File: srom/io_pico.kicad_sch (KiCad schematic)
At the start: 3 parts, among them U201 Pico-rp2040

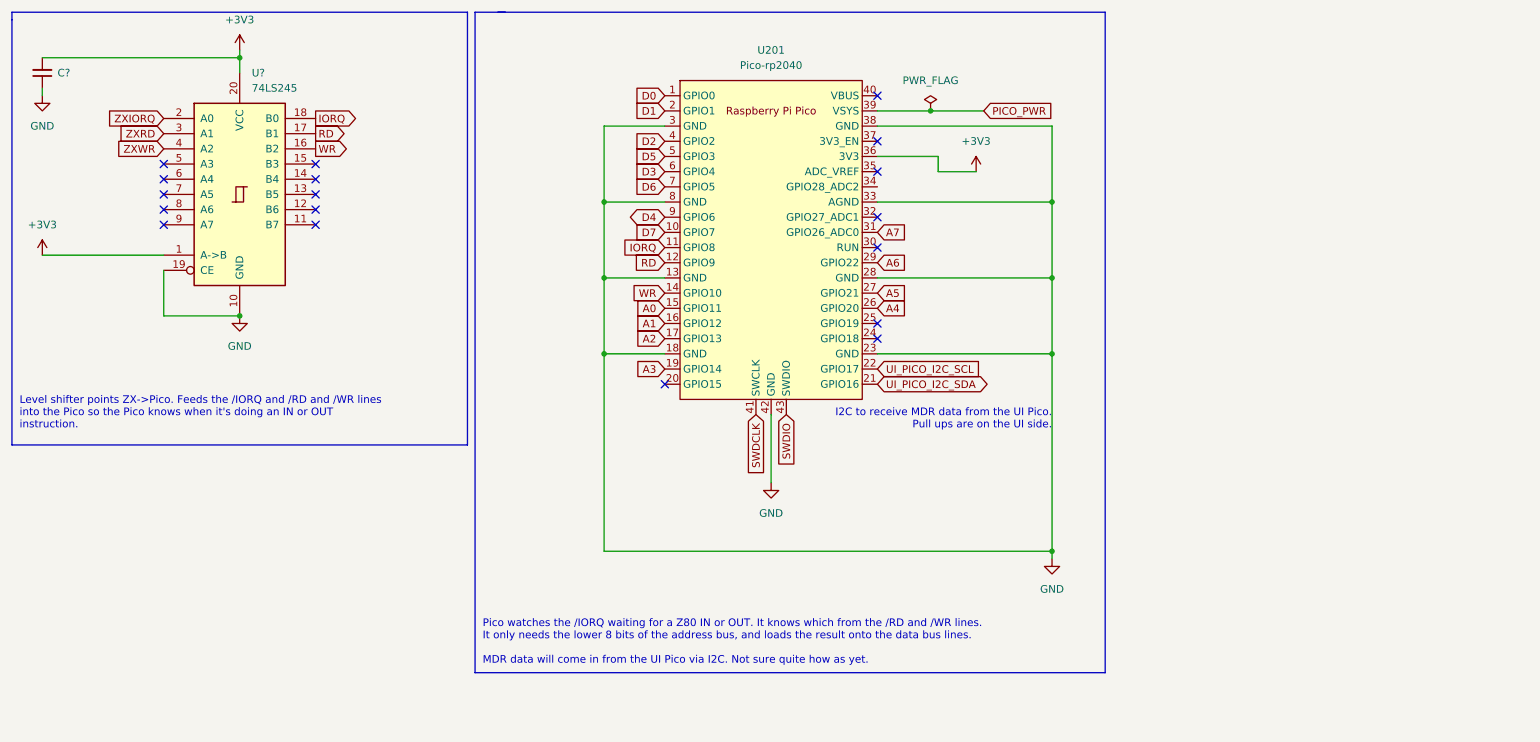
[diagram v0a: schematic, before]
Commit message: schematics complete for IO and UI picos
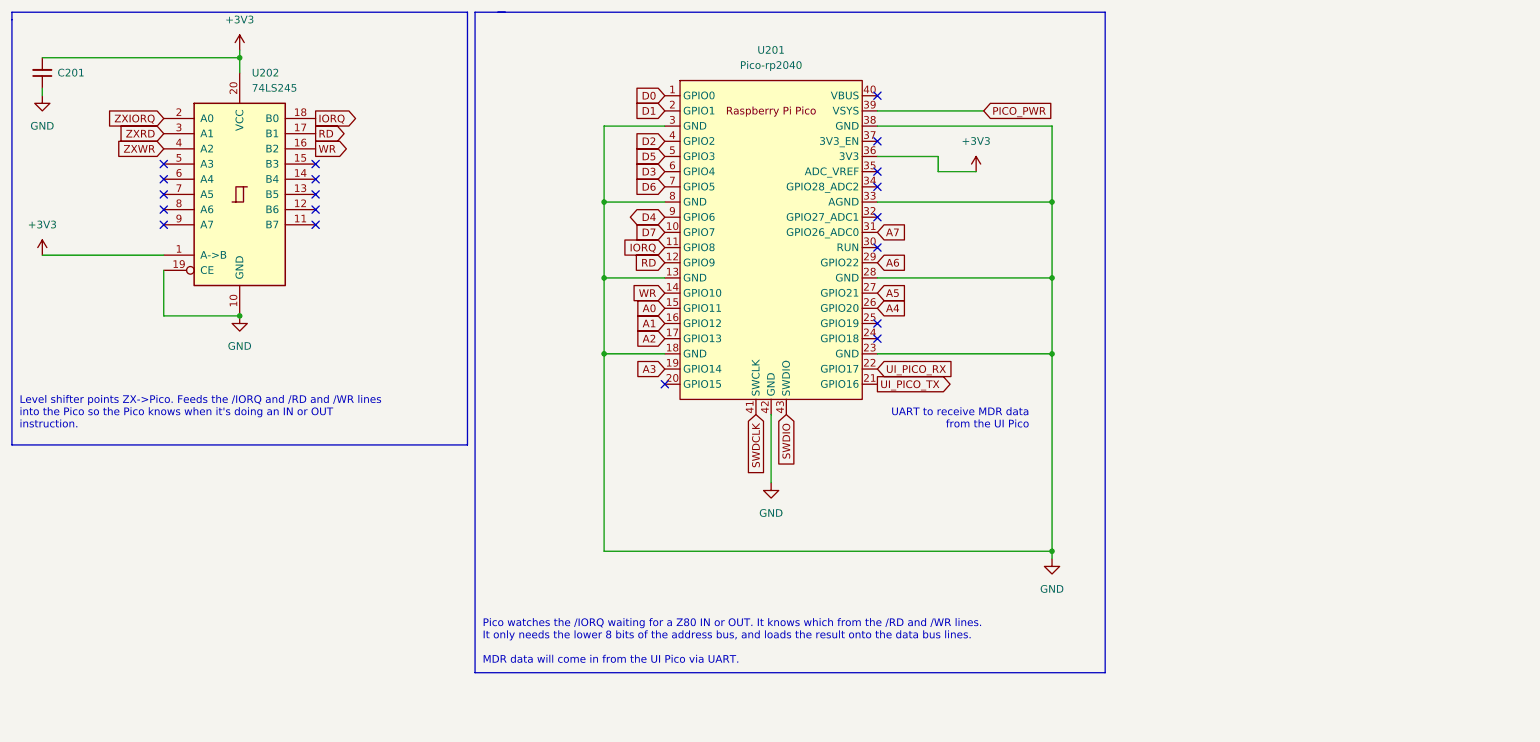
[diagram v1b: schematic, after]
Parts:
- gave numbers to parts that had none: 2
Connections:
- net UI_PICO_I2C_SCL renamed UI_PICO_RX
- net UI_PICO_I2C_SDA renamed UI_PICO_TX
- no-connect marks 18 -> 19
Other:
- note added: "Pico watches the /IORQ waiting for a Z80 IN or OUT. It knows which from the /RD and /WR lines. It only needs the lower 8 bits of the address bus, and loads the result onto the data bus lines. MDR data will come in from the UI Pico via UART."
- note added: "UART to receive MDR data from the UI Pico"
- note removed: "I2C to receive MDR data from the UI Pico. Pull ups are on the UI side."
- note removed: "Pico watches the /IORQ waiting for a Z80 IN or OUT. It knows which from the /RD and /WR lines. It only needs the lower 8 bits of the address bus, and loads the result onto the data bus lines. MDR data will come in from the UI Pico via I2C. Not sure quite how as yet."
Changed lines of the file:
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@@
   (junction (at 191.77 80.01) (diameter 0) (color 0 0 0 0)
-  )
-  (junction (at 171.45 52.07) (diameter 0) (color 0 0 0 0)
   )
   (no_connect (at 162.56 49.53))
@@
   (no_connect (at 43.18 68.58))
   (no_connect (at 127 97.79))
+  (no_connect (at 162.56 64.77))
   (no_connect (at 162.56 62.23))
   (no_connect (at 43.18 60.96))
@@
     (stroke (width 0) (type default) (color 0 0 0 0))
   )
-  (wire (pts (xy 162.56 52.07) (xy 171.45 52.07))
-    (stroke (width 0) (type default) (color 0 0 0 0))
-  )
   (polyline (pts (xy 17.78 35.56) (xy 17.78 36.83))
     (stroke (width 0) (type default) (color 0 0 0 0))
@@
     (stroke (width 0) (type default) (color 0 0 0 0))
   )
-  (wire (pts (xy 171.45 52.07) (xy 180.34 52.07))
+  (wire (pts (xy 162.56 52.07) (xy 180.34 52.07))
     (stroke (width 0) (type default) (color 0 0 0 0))
   )
@@
     (stroke (width 0) (type default) (color 0 0 0 0))
   )
-  (text "I2C to receive MDR data from the UI Pico.\nPull ups are on the UI side."
-    (at 191.77 105.41 180)
+  (text "UART to receive MDR data\nfrom the UI Pico" (at 187.96 105.41 180)
     (effects (font (size 1.27 1.27)) (justify right bottom))
   )
@@
     (effects (font (size 1.27 1.27)) (justify left bottom))
   )
-  (text "Pico watches the /IORQ waiting for a Z80 IN or OUT. It knows which from the /RD and /WR lines.\nIt only needs the lower 8 bits of the address bus, and loads the result onto the data bus lines.\n\nMDR data will come in from the UI Pico via I2C. Not sure quite how as yet."
+  (text "Pico watches the /IORQ waiting for a Z80 IN or OUT. It knows which from the /RD and /WR lines.\nIt only needs the lower 8 bits of the address bus, and loads the result onto the data bus lines.\n\nMDR data will come in from the UI Pico via UART."
     (at 96.52 144.78 0)
     (effects (font (size 1.27 1.27)) (justify left bottom))
@@
     )
   )
-  (global_label "UI_PICO_I2C_SCL" (shape input) (at 162.56 95.25 0) (fields_autoplaced)
-    (effects (font (size 1.27 1.27)) (justify left))
-    (property "Intersheet References" "${INTERSHEET_REFS}" (id 0) (at 180.8783 95.1706 0)
+  (global_label "UI_PICO_RX" (shape input) (at 162.56 95.25 0) (fields_autoplaced)
+    (effects (font (size 1.27 1.27)) (justify left))
+    (property "Intersheet References" "${INTERSHEET_REFS}" (id 0) (at 175.7983 95.1706 0)
       (effects (font (size 1.27 1.27)) (justify left) hide)
     )
@@
     )
   )
-  (global_label "UI_PICO_I2C_SDA" (shape bidirectional) (at 162.56 97.79 0) (fields_autoplaced)
-    (effects (font (size 1.27 1.27)) (justify left))
-    (property "Intersheet References" "${INTERSHEET_REFS}" (id 0) (at 180.9388 97.7106 0)
+  (global_label "UI_PICO_TX" (shape output) (at 162.56 97.79 0) (fields_autoplaced)
+    (effects (font (size 1.27 1.27)) (justify left))
+    (property "Intersheet References" "${INTERSHEET_REFS}" (id 0) (at 175.496 97.7106 0)
       (effects (font (size 1.27 1.27)) (justify left) hide)
     )
@@
   (symbol (lib_id "power:+3V3") (at 22.86 76.2 0) (unit 1)
     (in_bom yes) (on_board yes) (fields_autoplaced)
-    (property "Reference" "#PWR?" (id 0) (at 22.86 80.01 0)
+    (property "Reference" "#PWR0205" (id 0) (at 22.86 80.01 0)
       (effects (font (size 1.27 1.27)) hide)
     )
@@
   (symbol (lib_name "74LS245_1") (lib_id "74xx:74LS245") (at 55.88 66.04 0) (unit 1)
     (in_bom yes) (on_board yes)
-    (property "Reference" "U?" (id 0) (at 57.8994 45.72 0)
+    (property "Reference" "U202" (id 0) (at 57.8994 45.72 0)
       (effects (font (size 1.27 1.27)) (justify left))
     )
@@
   (symbol (lib_id "Device:C_Small") (at 22.86 45.72 180) (unit 1)
     (in_bom yes) (on_board yes) (fields_autoplaced)
-    (property "Reference" "C?" (id 0) (at 25.4 45.7135 0)
+    (property "Reference" "C201" (id 0) (at 25.4 45.7135 0)
       (effects (font (size 1.27 1.27)) (justify right))
     )
@@
   (symbol (lib_id "power:GND") (at 55.88 86.36 0) (unit 1)
     (in_bom yes) (on_board yes) (fields_autoplaced)
-    (property "Reference" "#PWR?" (id 0) (at 55.88 92.71 0)
+    (property "Reference" "#PWR0207" (id 0) (at 55.88 92.71 0)
       (effects (font (size 1.27 1.27)) hide)
     )
@@
     )
     (property "Datasheet" "" (id 3) (at 55.88 86.36 0)
-      (effects (font (size 1.27 1.27)) hide)
-    )
-    (pin "1")
-  )
-  (symbol (lib_id "power:PWR_FLAG") (at 171.45 52.07 0) (unit 1)
-    (in_bom yes) (on_board yes) (fields_autoplaced)
-    (property "Reference" "#FLG0201" (id 0) (at 171.45 50.165 0)
-      (effects (font (size 1.27 1.27)) hide)
-    )
-    (property "Value" "PWR_FLAG" (id 1) (at 171.45 46.99 0))
-    (property "Footprint" "" (id 2) (at 171.45 52.07 0)
-      (effects (font (size 1.27 1.27)) hide)
-    )
-    (property "Datasheet" "~" (id 3) (at 171.45 52.07 0)
       (effects (font (size 1.27 1.27)) hide)
     )
@@
   (symbol (lib_id "power:+3V3") (at 55.88 41.91 0) (unit 1)
     (in_bom yes) (on_board yes) (fields_autoplaced)
-    (property "Reference" "#PWR?" (id 0) (at 55.88 45.72 0)
+    (property "Reference" "#PWR0206" (id 0) (at 55.88 45.72 0)
       (effects (font (size 1.27 1.27)) hide)
     )
@@
   (symbol (lib_id "power:GND") (at 22.86 49.53 0) (unit 1)
     (in_bom yes) (on_board yes)
-    (property "Reference" "#PWR?" (id 0) (at 22.86 55.88 0)
-      (effects (font (size 1.27 1.27)) hide)
-    )
+    (property "Reference" "#PWR0204" (id 0) (at 22.86 55.88 0)
+      (effects (font (size 1.27 1.27)) hide)
+    )

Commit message: first draft pcb layout
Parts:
- added J201: Conn_01x03_Female, Connector_PinHeader_2.54mm:PinHeader_1x03_P2.54mm_Vertical, symbol Connector:Conn_01x03_Female
- U201: value Pico-rp2040 -> Pico-2 IO
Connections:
- net GND: now also J201.2 (Pin_2)
- net SWDCLK renamed SWDCLK_P2
- net SWDCLK_P2: now also J201.3 (Pin_3)
- net SWDIO renamed SWDIO_P2
- net SWDIO_P2: now also J201.1 (Pin_1)
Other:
- note added: "STLINK-V2 programming connector"
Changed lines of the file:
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@@
+    (stroke (width 0) (type default) (color 0 0 0 0))
+  )
+  (wire (pts (xy 241.3 111.125) (xy 241.3 109.855))
     (stroke (width 0) (type default) (color 0 0 0 0))
   )
@@
   )
   (polyline (pts (xy 17.78 36.83) (xy 17.78 36.83))
+    (stroke (width 0) (type default) (color 0 0 0 0))
+  )
+  (wire (pts (xy 241.3 109.855) (xy 225.425 109.855))
     (stroke (width 0) (type default) (color 0 0 0 0))
   )
@@
     (effects (font (size 1.27 1.27)) (justify left bottom))
   )
+  (text "STLINK-V2 programming connector" (at 207.01 100.33 0)
+    (effects (font (size 1.27 1.27)) (justify left bottom))
+  )
   (global_label "A0" (shape input) (at 127 85.09 180) (fields_autoplaced)
     (effects (font (size 1.27 1.27)) (justify right))
@@
     )
   )
-  (global_label "SWDCLK" (shape input) (at 142.24 102.87 270) (fields_autoplaced)
-    (effects (font (size 1.27 1.27)) (justify right))
-    (property "Intersheet References" "${INTERSHEET_REFS}" (id 0) (at 261.62 -54.61 0)
-      (effects (font (size 1.27 1.27)) hide)
-    )
-  )
-  (global_label "SWDIO" (shape input) (at 147.32 102.87 270) (fields_autoplaced)
-    (effects (font (size 1.27 1.27)) (justify right))
-    (property "Intersheet References" "${INTERSHEET_REFS}" (id 0) (at 261.62 -54.61 0)
-      (effects (font (size 1.27 1.27)) hide)
+  (global_label "SWDCLK_P2" (shape input) (at 142.24 102.87 270) (fields_autoplaced)
+    (effects (font (size 1.27 1.27)) (justify right))
+    (property "Intersheet References" "${INTERSHEET_REFS}" (id 0) (at 142.1606 116.2293 90)
+      (effects (font (size 1.27 1.27)) (justify right) hide)
+    )
+  )
+  (global_label "SWDIO_P2" (shape input) (at 225.425 107.315 0) (fields_autoplaced)
+    (effects (font (size 1.27 1.27)) (justify left))
+    (property "Intersheet References" "${INTERSHEET_REFS}" (id 0) (at 237.1514 107.2356 0)
+      (effects (font (size 1.27 1.27)) (justify left) hide)
+    )
+  )
+  (global_label "SWDCLK_P2" (shape input) (at 225.425 112.395 0) (fields_autoplaced)
+    (effects (font (size 1.27 1.27)) (justify left))
+    (property "Intersheet References" "${INTERSHEET_REFS}" (id 0) (at 238.7843 112.3156 0)
+      (effects (font (size 1.27 1.27)) (justify left) hide)
+    )
+  )
+  (global_label "SWDIO_P2" (shape input) (at 147.32 102.87 270) (fields_autoplaced)
+    (effects (font (size 1.27 1.27)) (justify right))
+    (property "Intersheet References" "${INTERSHEET_REFS}" (id 0) (at 147.2406 114.5964 90)
+      (effects (font (size 1.27 1.27)) (justify right) hide)
     )
   )
@@
     (pin "1")
   )
+  (symbol (lib_id "Connector:Conn_01x03_Female") (at 220.345 109.855 0) (mirror y) (unit 1)
+    (in_bom yes) (on_board yes)
+    (property "Reference" "J201" (id 0) (at 223.0882 102.616 0))
+    (property "Value" "Conn_01x03_Female" (id 1) (at 223.0882 104.9274 0))
+    (property "Footprint" "Connector_PinHeader_2.54mm:PinHeader_1x03_P2.54mm_Vertical" (id 2) (at 220.345 109.855 0)
+      (effects (font (size 1.27 1.27)) hide)
+    )
+    (property "Datasheet" "~" (id 3) (at 220.345 109.855 0)
+      (effects (font (size 1.27 1.27)) hide)
+    )
+    (pin "1")
+    (pin "2")
+    (pin "3")
+  )
+  (symbol (lib_id "power:GND") (at 241.3 111.125 0) (mirror y) (unit 1)
+    (in_bom yes) (on_board yes)
+    (property "Reference" "#PWR0208" (id 0) (at 241.3 117.475 0)
+      (effects (font (size 1.27 1.27)) hide)
+    )
+    (property "Value" "GND" (id 1) (at 241.173 115.5192 0))
+    (property "Footprint" "" (id 2) (at 241.3 111.125 0)
+      (effects (font (size 1.27 1.27)) hide)
+    )
+    (property "Datasheet" "" (id 3) (at 241.3 111.125 0)
+      (effects (font (size 1.27 1.27)) hide)
+    )
+    (pin "1")
+  )
   (symbol (lib_id "power:GND") (at 191.77 127 0) (unit 1)
     (in_bom yes) (on_board yes) (fields_autoplaced)
@@
     (in_bom yes) (on_board yes) (fields_autoplaced)
     (property "Reference" "U201" (id 0) (at 144.78 41.91 0))
-    (property "Value" "Pico-rp2040" (id 1) (at 144.78 44.45 0))
+    (property "Value" "Pico-2 IO" (id 1) (at 144.78 44.45 0))
     (property "Footprint" "pico-foot:RPi_Pico_SMD_TH" (id 2) (at 144.78 73.66 90)
       (effects (font (size 1.27 1.27)) hide)

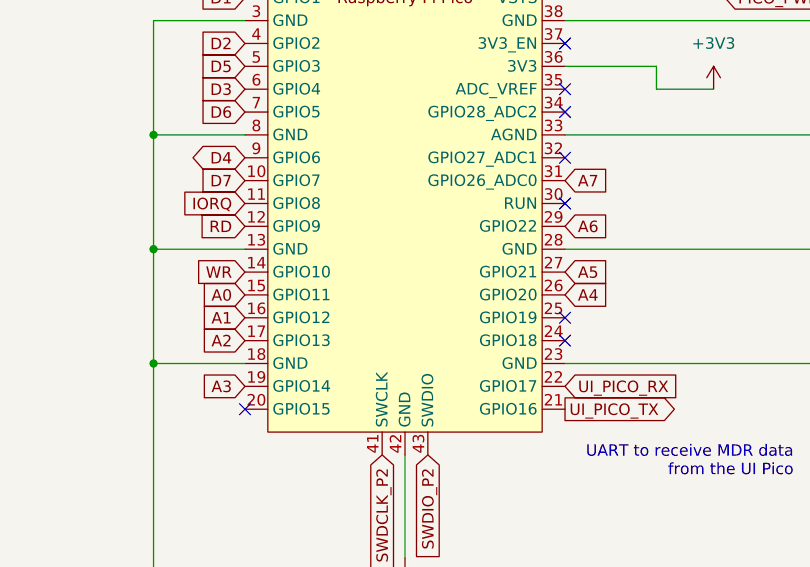
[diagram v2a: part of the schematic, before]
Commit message: update schema and layout to match working ROM emulation board. 2 level shifters removed here
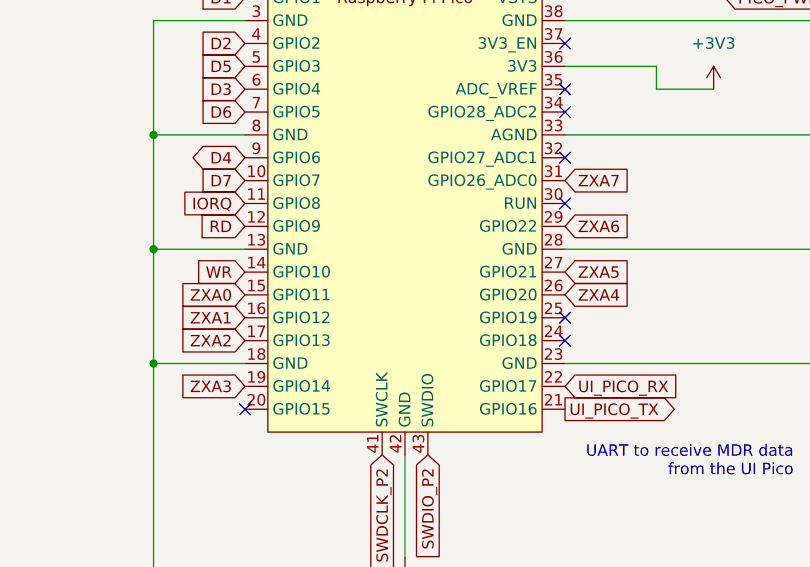
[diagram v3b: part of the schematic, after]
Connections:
- net A0 renamed ZXA0
- net A1 renamed ZXA1
- net A2 renamed ZXA2
- net A3 renamed ZXA3
- net A4 renamed ZXA4
- net A5 renamed ZXA5
- net A6 renamed ZXA6
- net A7 renamed ZXA7
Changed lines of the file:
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@@
     (effects (font (size 1.27 1.27)) (justify left bottom))
   )
-  (global_label "A0" (shape input) (at 127 85.09 180) (fields_autoplaced)
+  (global_label "ZXA0" (shape input) (at 127 85.09 180) (fields_autoplaced)
     (effects (font (size 1.27 1.27)) (justify right))
-    (property "Intersheet References" "${INTERSHEET_REFS}" (id 0) (at 122.2888 85.0106 0)
+    (property "Intersheet References" "${INTERSHEET_REFS}" (id 0) (at 119.8698 85.0106 0)
       (effects (font (size 1.27 1.27)) (justify right) hide)
     )
@@
     )
   )
-  (global_label "A5" (shape input) (at 162.56 82.55 0) (fields_autoplaced)
+  (global_label "ZXA5" (shape input) (at 162.56 82.55 0) (fields_autoplaced)
     (effects (font (size 1.27 1.27)) (justify left))
-    (property "Intersheet References" "${INTERSHEET_REFS}" (id 0) (at 167.2712 82.4706 0)
+    (property "Intersheet References" "${INTERSHEET_REFS}" (id 0) (at 169.6902 82.4706 0)
       (effects (font (size 1.27 1.27)) (justify left) hide)
     )
@@
     )
   )
-  (global_label "A2" (shape input) (at 127 90.17 180) (fields_autoplaced)
+  (global_label "ZXA2" (shape input) (at 127 90.17 180) (fields_autoplaced)
     (effects (font (size 1.27 1.27)) (justify right))
-    (property "Intersheet References" "${INTERSHEET_REFS}" (id 0) (at 122.2888 90.0906 0)
+    (property "Intersheet References" "${INTERSHEET_REFS}" (id 0) (at 119.8698 90.0906 0)
       (effects (font (size 1.27 1.27)) (justify right) hide)
     )
@@
     )
   )
-  (global_label "A1" (shape input) (at 127 87.63 180) (fields_autoplaced)
+  (global_label "ZXA1" (shape input) (at 127 87.63 180) (fields_autoplaced)
     (effects (font (size 1.27 1.27)) (justify right))
-    (property "Intersheet References" "${INTERSHEET_REFS}" (id 0) (at 122.2888 87.5506 0)
+    (property "Intersheet References" "${INTERSHEET_REFS}" (id 0) (at 119.8698 87.5506 0)
       (effects (font (size 1.27 1.27)) (justify right) hide)
     )
   )
-  (global_label "A3" (shape input) (at 127 95.25 180) (fields_autoplaced)
+  (global_label "ZXA3" (shape input) (at 127 95.25 180) (fields_autoplaced)
     (effects (font (size 1.27 1.27)) (justify right))
-    (property "Intersheet References" "${INTERSHEET_REFS}" (id 0) (at 122.2888 95.1706 0)
+    (property "Intersheet References" "${INTERSHEET_REFS}" (id 0) (at 119.8698 95.1706 0)
       (effects (font (size 1.27 1.27)) (justify right) hide)
     )
@@
     )
   )
-  (global_label "A4" (shape input) (at 162.56 85.09 0) (fields_autoplaced)
+  (global_label "ZXA4" (shape input) (at 162.56 85.09 0) (fields_autoplaced)
     (effects (font (size 1.27 1.27)) (justify left))
-    (property "Intersheet References" "${INTERSHEET_REFS}" (id 0) (at 167.2712 85.0106 0)
+    (property "Intersheet References" "${INTERSHEET_REFS}" (id 0) (at 169.6902 85.0106 0)
       (effects (font (size 1.27 1.27)) (justify left) hide)
     )
@@
     )
   )
-  (global_label "A6" (shape input) (at 162.56 77.47 0) (fields_autoplaced)
+  (global_label "ZXA6" (shape input) (at 162.56 77.47 0) (fields_autoplaced)
     (effects (font (size 1.27 1.27)) (justify left))
-    (property "Intersheet References" "${INTERSHEET_REFS}" (id 0) (at 167.2712 77.3906 0)
+    (property "Intersheet References" "${INTERSHEET_REFS}" (id 0) (at 169.6902 77.3906 0)
       (effects (font (size 1.27 1.27)) (justify left) hide)
     )
   )
-  (global_label "A7" (shape input) (at 162.56 72.39 0) (fields_autoplaced)
+  (global_label "ZXA7" (shape input) (at 162.56 72.39 0) (fields_autoplaced)
     (effects (font (size 1.27 1.27)) (justify left))
-    (property "Intersheet References" "${INTERSHEET_REFS}" (id 0) (at 167.2712 72.3106 0)
+    (property "Intersheet References" "${INTERSHEET_REFS}" (id 0) (at 169.6902 72.3106 0)
       (effects (font (size 1.27 1.27)) (justify left) hide)
     )
